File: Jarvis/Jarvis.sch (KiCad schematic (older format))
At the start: 124 parts, among them IC1 ADP1607, IC2 MAX-8Q, IC3 MPU-9250, IC4 STM32F411CxUx, IC5 Si4460, IC6 MS5611-01BA03, IC7 S25FL127S, J1 PYRO, J2 PWR, J3 ARM, J4 MICROUSB, P1 SMA, P2 SMA, P3 SWD_TC, Q1 PFET, Q2 PFET, Q3 PFET, Q4 NFET, Q5 NFET, Q6 NFET, Q7 NFET, X1 434MHz ANT, X10 Housing x1, X11 Housing x3, X12 M Crimps x6, X13 F Crimps x17, X14 Crimp Tool, X2 Red LED, X3 AA Battery, X4 AA Holder, X5 ARM Switch, X6 Wire, X7 Heat Shrink, X8 Housing x1, X9 Housing x4, Y1 26MHz, Y2 30MHz

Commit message: Schematic Complete
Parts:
- added R27, R28: 10k, agg:0402-L, symbol R_Small
- added R29: 100R, agg:0402-L, symbol R_Small
- added TP1, TP10, TP11, TP12, TP13, TP14, TP15, TP16, TP17, TP18, TP19, TP2, TP20, TP21, TP22, TP23, TP24, TP25, TP26, TP27, TP28, TP29, TP3, TP30, TP31, TP32, TP33, TP34, TP35, TP36, TP37, TP38, TP39, TP4, TP40, TP41, TP42, TP43, TP44, TP45, TP46, TP47, TP48, TP5, TP6, TP7, TP8, TP9: TESTPAD, agg:TESTPAD, symbol TESTPAD
- IC3: RS 883-7942P -> 883-7942
- LS1: footprint Library:ABI-042-RC -> Library:AI-1027-TWT-3V-R; Digikey (none) -> AI-1027-TWT-3V-R; Farnell 1827949 -> (none)
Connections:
- net 3v3: now also TP29.1 (TP), TP34.1 (TP), TP35.1 (TP), TP4.1 (TP), TP46.1 (TP), TP5.1 (TP)
- net BEEPER: now also TP40.1 (TP)
- net GND: now also R28.2, TP11.1 (TP), TP20.1 (TP), TP21.1 (TP), TP22.1 (TP)
- net GPS_RST: now also TP23.1 (TP)
- net I2C1_SCL: now also TP48.1 (TP)
- net I2C1_SDA: now also TP47.1 (TP)
- net MPU_IRQ: now also TP32.1 (TP)
- net PYRO1: now also TP16.1 (TP)
- net PYRO1_F: now also TP12.1 (TP)
- net PYRO1_S: now also TP24.1 (TP)
- net PYRO2: now also TP17.1 (TP)
- net PYRO2_F: now also TP13.1 (TP)
- net PYRO2_S: now also TP25.1 (TP)
- net PYRO3: now also TP18.1 (TP)
- net PYRO3_F: now also TP14.1 (TP)
- net PYRO3_S: now also TP26.1 (TP)
- net PYRO_SO: now also TP1.1 (TP), TP2.1 (TP), TP3.1 (TP)
- net Radio_nIRQ: now also TP43.1 (TP)
- net SPI1_MISO: now also TP37.1 (TP), TP42.1 (TP)
- net SPI1_MOSI: now also TP39.1 (TP), TP45.1 (TP)
- net SPI1_NSS1_FLASH: now also TP33.1 (TP)
- net SPI1_NSS2_RADIO: now also IC4.29 (PA8), TP44.1 (TP); no longer IC4.13 (PA3)
- net SPI1_SCK: now also TP36.1 (TP), TP41.1 (TP)
- net SPI2_MISO: now also TP27.1 (TP)
- net SPI2_MOSI: now also TP30.1 (TP)
- net SPI2_NSS1_MPU: now also TP28.1 (TP)
- net SPI2_SCK: now also TP31.1 (TP)
- net USART1_RX: now also TP15.1 (TP)
- net USART1_TX: now also TP19.1 (TP)
- net VBATT: now also R27.1, TP6.1 (TP)
- net at LS1.2, R33.1: now also R29.1
- net at Q7.3 (D), R33.2: now also R29.2, TP38.1 (TP)
- net at Q4.3 (D), R4.1: now also TP7.1 (TP)
- net at Q5.3 (D), R5.1: now also TP8.1 (TP)
- net at Q6.3 (D), R6.1: now also TP9.1 (TP)
- new net BATT_MON: IC4.13 (PA3), R27.2, R28.1, TP10.1 (TP)
- no-connect marks 25 -> 24
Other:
- note added: "100R"
- note added: "138 Hours"
- note added: "21.6 mA"
- note added: "Id = 3.3v / (1/(0.01 + 0.01) + 100 + 2.8) = 21.6 mA \nPower = 3.3v * 21.6 mA = 71 mW\n21.6 mA @ 3000 mAh -> 138 Hours"
- note removed: "150 Hours"
- note removed: "18.6 mA"
- note removed: "75R"
- note removed: "Id = 3.3v / (75 + 100 + 2.8) = 18.6 mA \nPower = 3.3v * 18.6 mA = 61 mW\n18.6 mA @ 3000 mAh -> 150 Hours"
- note removed: "TODO: Add Test Points"
- moved on the sheet: LS1, R33

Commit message: Routing progress
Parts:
- added X?: RF Frame, symbol PART
- added X?: RF Cover, symbol PART
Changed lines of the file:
@@
 	-1   0    0    1
 $EndComp
+$Comp
+L PART X?
+U 1 1 5709D0FD
+P 6400 5900
+F 0 "X?" H 6450 6000 50  0000 L CNN
+F 1 "RF Frame" H 6450 5900 45  0000 L CNN
+F 2 "" H 6400 5900 50  0001 C CNN
+F 3 "http://media.digikey.com/pdf/Data%20Sheets/Laird%20Technologies/BMI-S-201-F_Dwg.pdf" H 6400 5900 50  0001 C CNN
+F 4 "BMI-S-201-F" H 6400 5900 60  0001 C CNN "Digikey"
+	1    6400 5900
+	1    0    0    -1
+$EndComp
+$Comp
+L PART X?
+U 1 1 5709E7BE
+P 7000 5900
+F 0 "X?" H 7050 6000 50  0000 L CNN
+F 1 "RF Cover" H 7050 5900 45  0000 L CNN
+F 2 "" H 7000 5900 50  0001 C CNN
+F 3 "http://dkc3.digikey.com/PDF/UK2011-EN/P0572.pdf" H 7000 5900 50  0001 C CNN
+F 4 "BMI-S-201-C" H 7000 5900 60  0001 C CNN "Digikey"
+	1    7000 5900
+	1    0    0    -1
+$EndComp
 $EndSCHEMATC

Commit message: Continued Layout
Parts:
- added C29: 100nF, agg:0402-L, symbol C_Small
- added TP49: TESTPAD, agg:TESTPAD, symbol TESTPAD
- C16: footprint agg:0603-L -> agg:0402-L; Farnell 2112849 -> 1759381
- X15: renamed from X?; footprint (none) -> Library:BMI-S-201-F
- gave numbers to parts that had none: 1
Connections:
- net 3v3: now also C29.1
- net GND: now also C29.2
- net FLASH_RST: now reaches IC4.20 (PB2)
- net FLASH_RST: now also IC7.7 (RST), TP49.1 (TP)
- no-connect marks 24 -> 22
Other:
- moved on the sheet: TP34, TP36, TP39
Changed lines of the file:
@@
 F 0 "C16" H 810 4670 50  0000 L CNN
 F 1 "1uF" H 810 4520 50  0000 L CNN
-F 2 "agg:0603-L" H 800 4600 50  0001 C CNN
-F 3 "http://www.farnell.com/datasheets/746258.pdf" H 800 4600 50  0001 C CNN
-F 4 "2112849" H 800 4600 60  0001 C CNN "Farnell"
+F 2 "agg:0402-L" H 800 4600 50  0001 C CNN
+F 3 "http://www.farnell.com/datasheets/1901289.pdf" H 800 4600 50  0001 C CNN
+F 4 "1759381" H 800 4600 60  0001 C CNN "Farnell"
 	1    800  4600
 	1    0    0    -1
@@
 $EndComp
 NoConn ~ 14650 6600
-NoConn ~ 15250 6500
 $Comp
 L 3v3 #PWR0114
 U 1 1 570704D3
-P 15350 6300
-F 0 "#PWR0114" H 15350 6410 50  0001 L CNN
-F 1 "3v3" H 15350 6390 50  0000 C CNN
-F 2 "" H 15350 6300 60  0000 C CNN
-F 3 "" H 15350 6300 60  0000 C CNN
-	1    15350 6300
+P 15300 6200
+F 0 "#PWR0114" H 15300 6310 50  0001 L CNN
+F 1 "3v3" H 15300 6290 50  0000 C CNN
+F 2 "" H 15300 6200 60  0000 C CNN
+F 3 "" H 15300 6200 60  0000 C CNN
+	1    15300 6200
 	1    0    0    -1
 $EndComp
@@
 Text Label 14550 6500 2    60   ~ 0
 SPI1_MISO
-Text Label 15350 6600 0    60   ~ 0
+Text Label 15400 6600 0    60   ~ 0
 SPI1_SCK
-Text Label 15350 6700 0    60   ~ 0
+Text Label 15400 6700 0    60   ~ 0
 SPI1_MOSI
 Text Label 3100 3950 0    60   ~ 0
@@
 Text Label 7150 3550 0    60   ~ 0
 SPI2_NSS1_MPU
-NoConn ~ 3000 5550
 NoConn ~ 3000 6250
 NoConn ~ 3000 6550
@@
 L TESTPAD TP39
 U 1 1 5710FB79
-P 15350 6800
-F 0 "TP39" H 15450 6800 50  0000 L CNN
-F 1 "TESTPAD" H 15350 6725 50  0001 L CNN
-F 2 "agg:TESTPAD" H 15350 6650 50  0001 L CNN
-F 3 "" H 15350 6800 50  0001 C CNN
-	1    15350 6800
+P 15400 6900
+F 0 "TP39" H 15500 6900 50  0000 L CNN
+F 1 "TESTPAD" H 15400 6825 50  0001 L CNN
+F 2 "agg:TESTPAD" H 15400 6750 50  0001 L CNN
+F 3 "" H 15400 6900 50  0001 C CNN
+	1    15400 6900
 	1    0    0    -1
 $EndComp
@@
 L TESTPAD TP36
 U 1 1 57112A68
-P 15350 6450
-F 0 "TP36" H 15450 6450 50  0000 L CNN
-F 1 "TESTPAD" H 15350 6375 50  0001 L CNN
-F 2 "agg:TESTPAD" H 15350 6300 50  0001 L CNN
-F 3 "" H 15350 6450 50  0001 C CNN
-	1    15350 6450
+P 15400 6800
+F 0 "TP36" H 15500 6800 50  0000 L CNN
+F 1 "TESTPAD" H 15400 6725 50  0001 L CNN
+F 2 "agg:TESTPAD" H 15400 6650 50  0001 L CNN
+F 3 "" H 15400 6800 50  0001 C CNN
+	1    15400 6800
 	1    0    0    -1
 $EndComp
@@
 	13000 6700 13000 6900
 Wire Wire Line
-	15250 6400 15350 6400
-Wire Wire Line
-	15350 6400 15350 6300
+	15300 6200 15300 6400
 Wire Wire Line
 	14550 6400 14650 6400
 Wire Wire Line
-	15250 6600 15350 6600
+	15250 6600 15400 6600
 Wire Wire Line
-	15250 6700 15350 6700
+	15250 6700 15400 6700
 Wire Wire Line
 	14550 6700 14550 6850
@@
 Connection ~ 14600 6400
 Wire Wire Line
-	15350 6450 15300 6450
-Wire Wire Line
-	15300 6450 15300 6600
-Connection ~ 15300 6600
-Wire Wire Line
-	15300 6700 15300 6800
-Wire Wire Line
-	15300 6800 15350 6800
+	15300 6700 15300 6900
 Connection ~ 15300 6700
 Wire Wire Line
@@
 L TESTPAD TP34
 U 1 1 57162848
-P 15400 6350
-F 0 "TP34" H 15500 6350 50  0000 L CNN
-F 1 "TESTPAD" H 15400 6275 50  0001 L CNN
-F 2 "agg:TESTPAD" H 15400 6200 50  0001 L CNN
-F 3 "" H 15400 6350 50  0001 C CNN
-	1    15400 6350
+P 15400 6250
+F 0 "TP34" H 15500 6250 50  0000 L CNN
+F 1 "TESTPAD" H 15400 6175 50  0001 L CNN
+F 2 "agg:TESTPAD" H 15400 6100 50  0001 L CNN
+F 3 "" H 15400 6250 50  0001 C CNN
+	1    15400 6250
 	1    0    0    -1
 $EndComp
-Wire Wire Line
-	15400 6350 15350 6350
-Connection ~ 15350 6350
+Connection ~ 15300 6250
 $Comp
 L TESTPAD TP5
@@
 $EndComp
 $Comp
-L PART X?
+L PART X15
 U 1 1 5709D0FD
 P 6400 5900
-F 0 "X?" H 6450 6000 50  0000 L CNN
+F 0 "X15" H 6450 6000 50  0000 L CNN
 F 1 "RF Frame" H 6450 5900 45  0000 L CNN
-F 2 "" H 6400 5900 50  0001 C CNN
+F 2 "Library:BMI-S-201-F" H 6400 5900 50  0001 C CNN
 F 3 "http://media.digikey.com/pdf/Data%20Sheets/Laird%20Technologies/BMI-S-201-F_Dwg.pdf" H 6400 5900 50  0001 C CNN
 F 4 "BMI-S-201-F" H 6400 5900 60  0001 C CNN "Digikey"
@@
 $EndComp
 $Comp
-L PART X?
+L PART X16
 U 1 1 5709E7BE
 P 7000 5900
-F 0 "X?" H 7050 6000 50  0000 L CNN
+F 0 "X16" H 7050 6000 50  0000 L CNN
 F 1 "RF Cover" H 7050 5900 45  0000 L CNN
 F 2 "" H 7000 5900 50  0001 C CNN
@@
 	1    0    0    -1
 $EndComp
+$Comp
+L 3v3 #PWR0118
+U 1 1 570B6059
+P 14950 7200
+F 0 "#PWR0118" H 14950 7310 50  0001 L CNN
+F 1 "3v3" H 14950 7290 50  0000 C CNN
+F 2 "" H 14950 7200 60  0000 C CNN
+F 3 "" H 14950 7200 60  0000 C CNN
+	1    14950 7200
+	1    0    0    -1
+$EndComp
+$Comp
+L GND #PWR0119
+U 1 1 570B605F
+P 14950 7400
+F 0 "#PWR0119" H 14950 7150 50  0001 C CNN
+F 1 "GND" H 14950 7250 50  0000 C CNN
+F 2 "" H 14950 7400 50  0000 C CNN
+F 3 "" H 14950 7400 50  0000 C CNN
+	1    14950 7400
+	1    0    0    -1
+$EndComp
+$Comp
+L C_Small C29
+U 1 1 570B6066
+P 14950 7300
+F 0 "C29" H 14960 7370 50  0000 L CNN
+F 1 "100nF" H 14960 7220 50  0000 L CNN
+F 2 "agg:0402-L" H 14950 7300 50  0001 C CNN
+F 3 "http://www.farnell.com/datasheets/1747441.pdf" H 14950 7300 50  0001 C CNN
+F 4 "1828860" H 14950 7300 60  0001 C CNN "Farnell"
+	1    14950 7300
+	1    0    0    -1
+$EndComp
+Wire Wire Line
+	15250 6500 15400 6500
+Wire Wire Line
+	15300 6250 15400 6250
+Text Label 15400 6500 0    60   ~ 0
+FLASH_RST
+Wire Wire Line
+	15300 6900 15400 6900
+Connection ~ 15350 6600
+Wire Wire Line
+	15300 6400 15250 6400
+Wire Wire Line
+	15350 6500 15350 6350
+Wire Wire Line
+	15350 6350 15400 6350
+Connection ~ 15350 6500
+$Comp
+L TESTPAD TP49
+U 1 1 570CB52B
+P 15400 6350
+F 0 "TP49" H 15500 6350 50  0000 L CNN
+F 1 "TESTPAD" H 15400 6275 50  0001 L CNN
+F 2 "agg:TESTPAD" H 15400 6200 50  0001 L CNN
+F 3 "" H 15400 6350 50  0001 C CNN
+	1    15400 6350
+	1    0    0    -1
+$EndComp
+Wire Wire Line
+	15400 6800 15350 6800
+Wire Wire Line
+	15350 6800 15350 6600
+Text Label 3100 5550 0    60   ~ 0
+FLASH_RST
+Wire Wire Line
+	3000 5550 3100 5550
 $EndSCHEMATC

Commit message: Continued PCB
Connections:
- net STAT_HBT: now also IC4.2 (PC13); no longer IC4.3 (PC14)
- net STAT_WRN: now also IC4.3 (PC14); no longer IC4.2 (PC13)
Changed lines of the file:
@@
 Text Label 2100 5450 2    60   ~ 0
 BEEPER
-Text Label 2100 5350 2    60   ~ 0
+Text Label 2100 5250 2    60   ~ 0
 STAT_HBT
 Text Notes 8650 4000 0    69   ~ 14
@@
 	1    0    0    -1
 $EndComp
-Text Label 2100 5250 2    60   ~ 0
+Text Label 2100 5350 2    60   ~ 0
 STAT_WRN
 $Comp

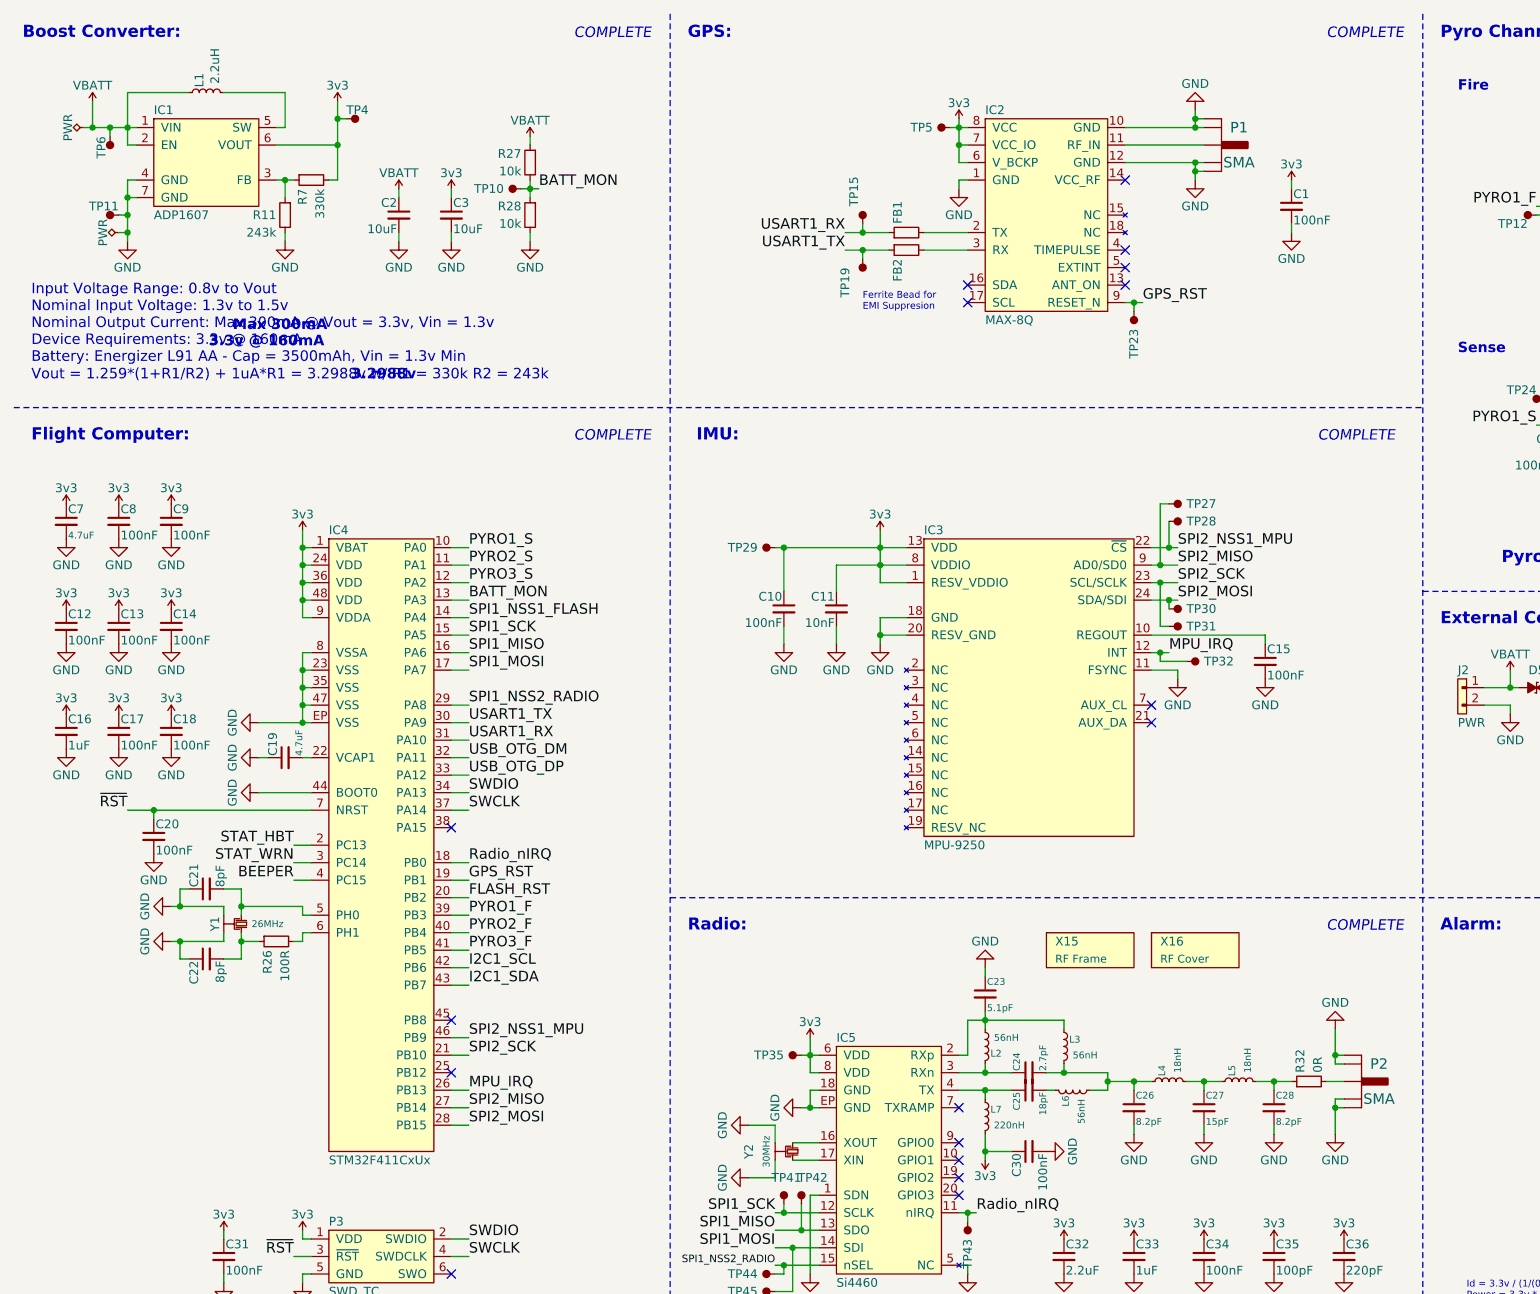
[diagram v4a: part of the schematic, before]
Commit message: Ready to Check Footprints
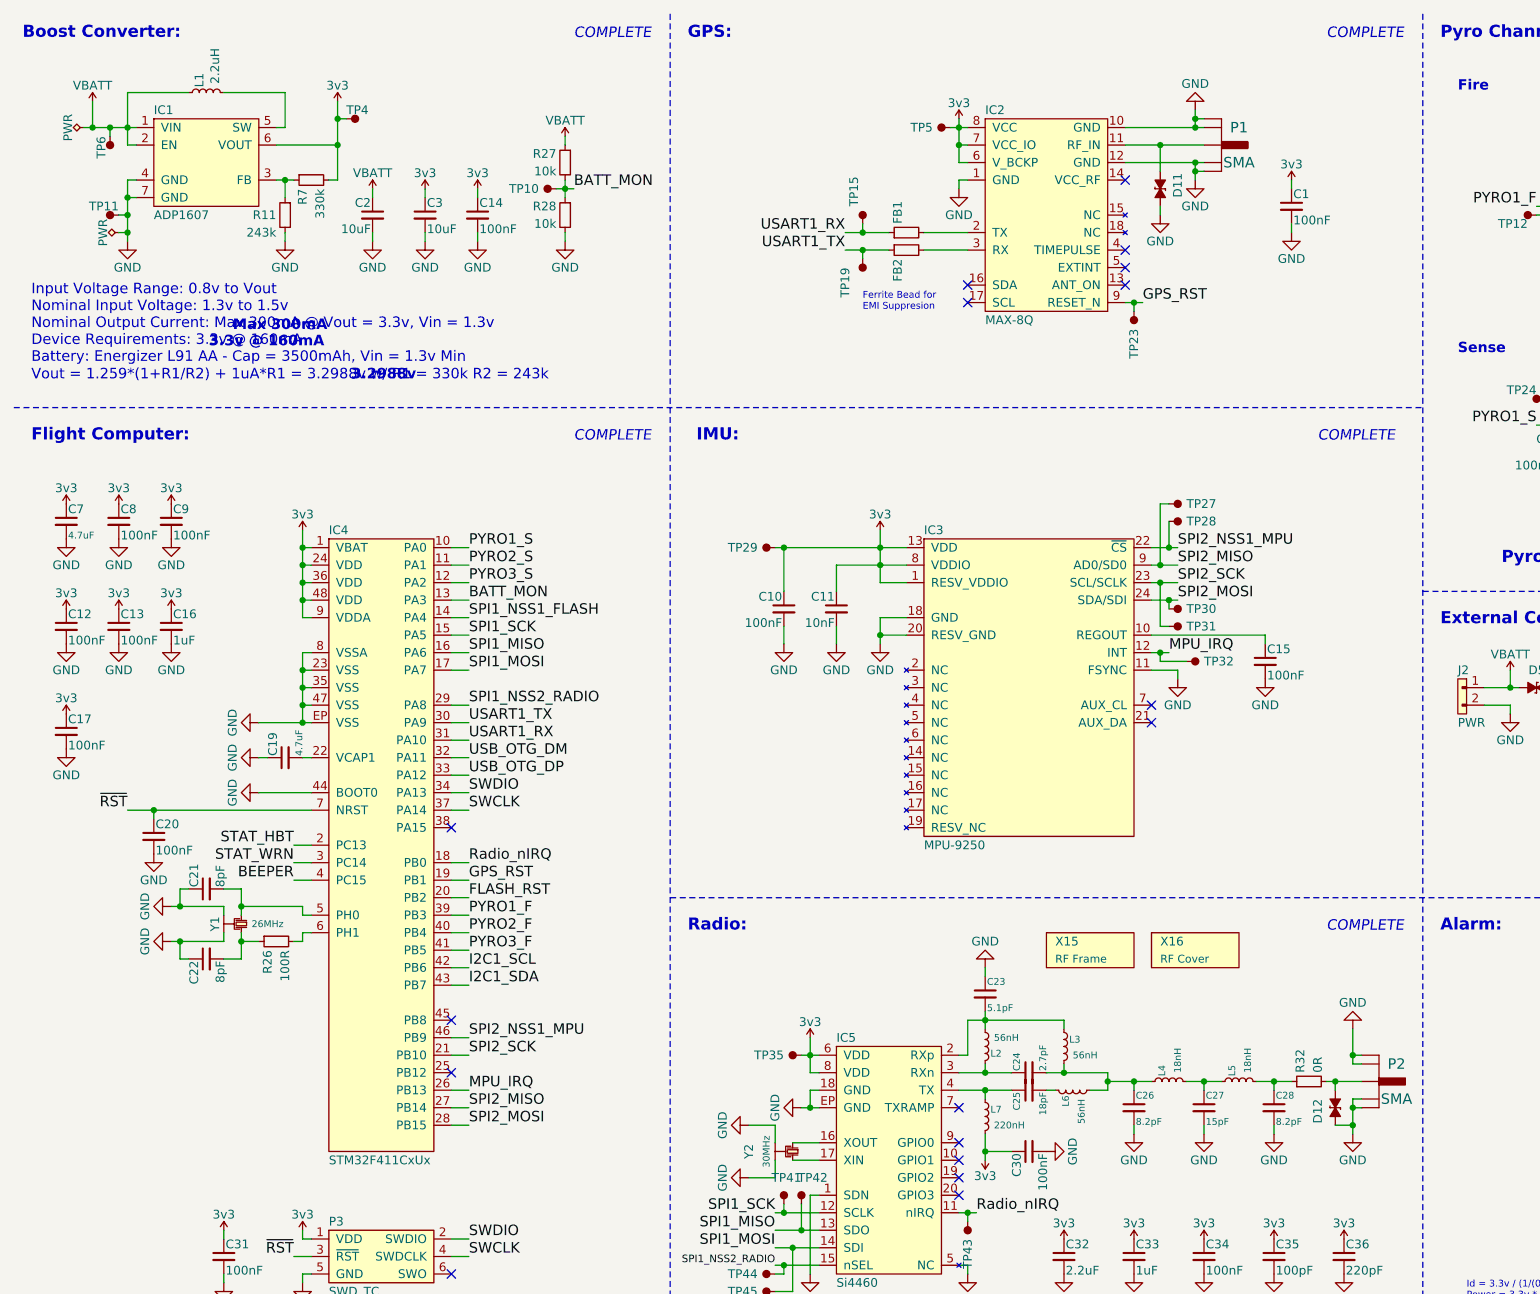
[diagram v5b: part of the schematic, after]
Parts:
- removed C18: 100nF, agg:0402-L, symbol C_Small
- added D11, D12: ESD_DIODE, agg:0402-L, symbol ESD_DIODE
- X15: Digikey BMI-S-201-F -> (none); Farnell (none) -> 2497715
- X16: Digikey BMI-S-201-C -> (none); Farnell (none) -> 2497714
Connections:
- net GND: now also D11.1, D12.2
- net at IC2.11 (RF_IN), P1.1 (RF): now also D11.2
- net at P2.1 (RF), R32.2: now also D12.1
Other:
- moved on the sheet: C14, C16, C2, C3, P2, R27, R28, TP10
